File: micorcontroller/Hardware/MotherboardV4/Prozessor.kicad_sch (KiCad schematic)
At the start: 56 parts, among them J4 GSB1C41110SSHR, Y2 ABM8G-12.000MHZ-4Y-T3

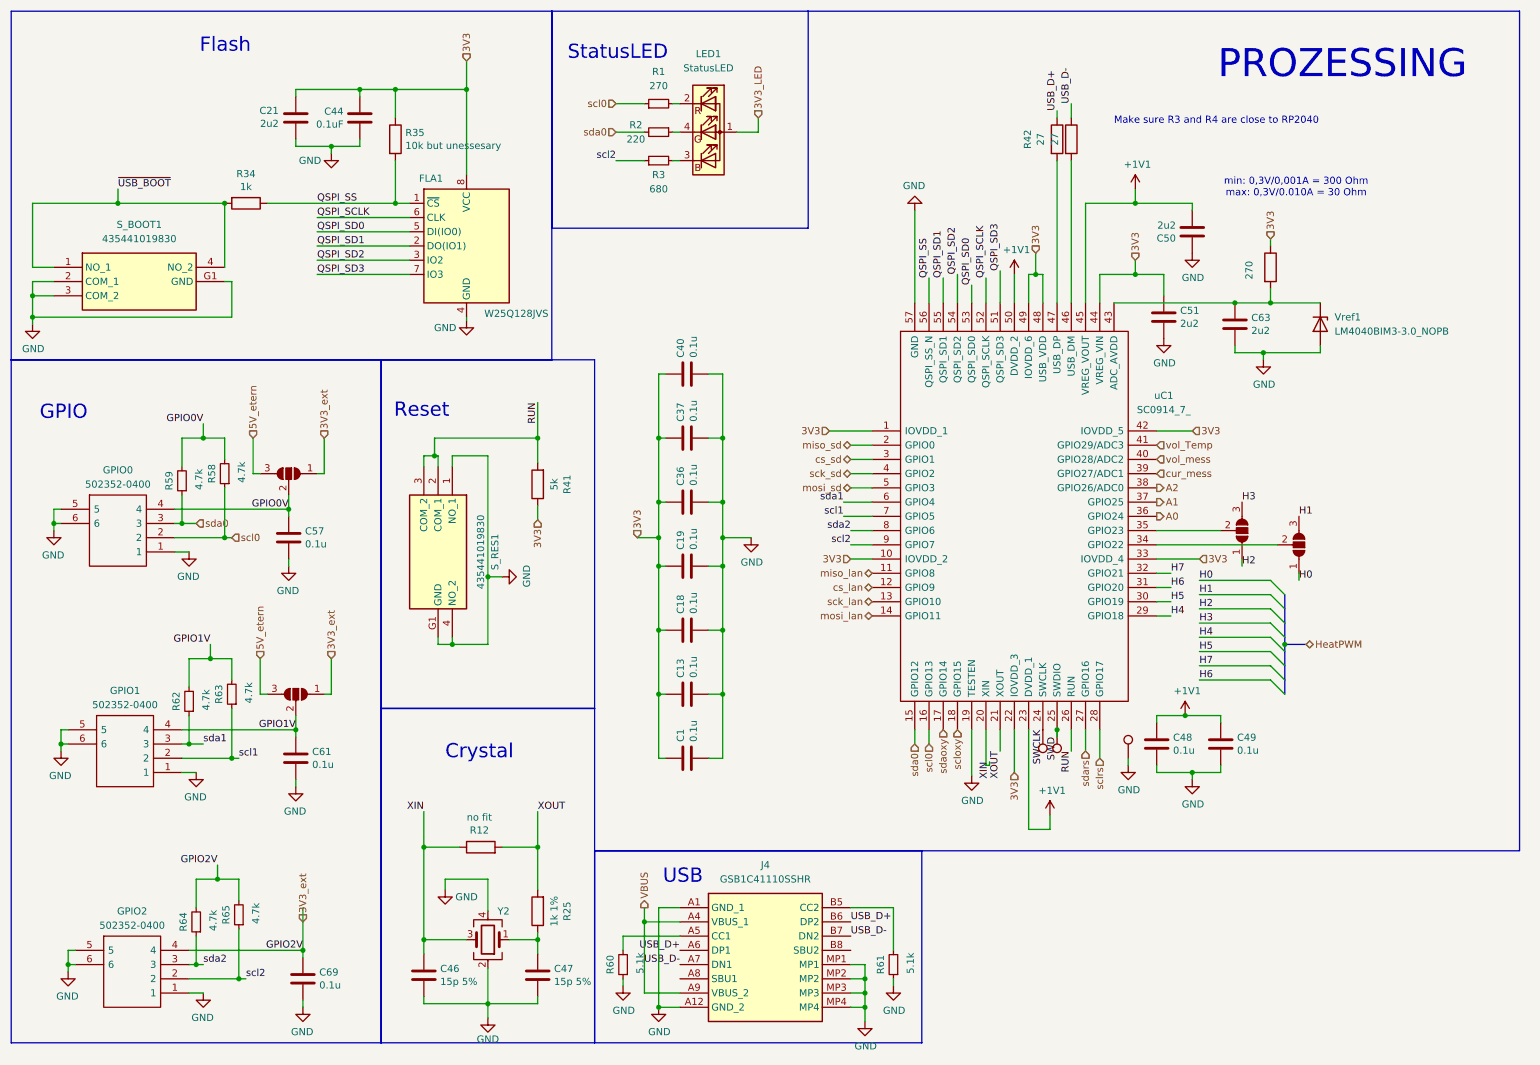
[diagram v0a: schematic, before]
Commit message: added NTC calculation
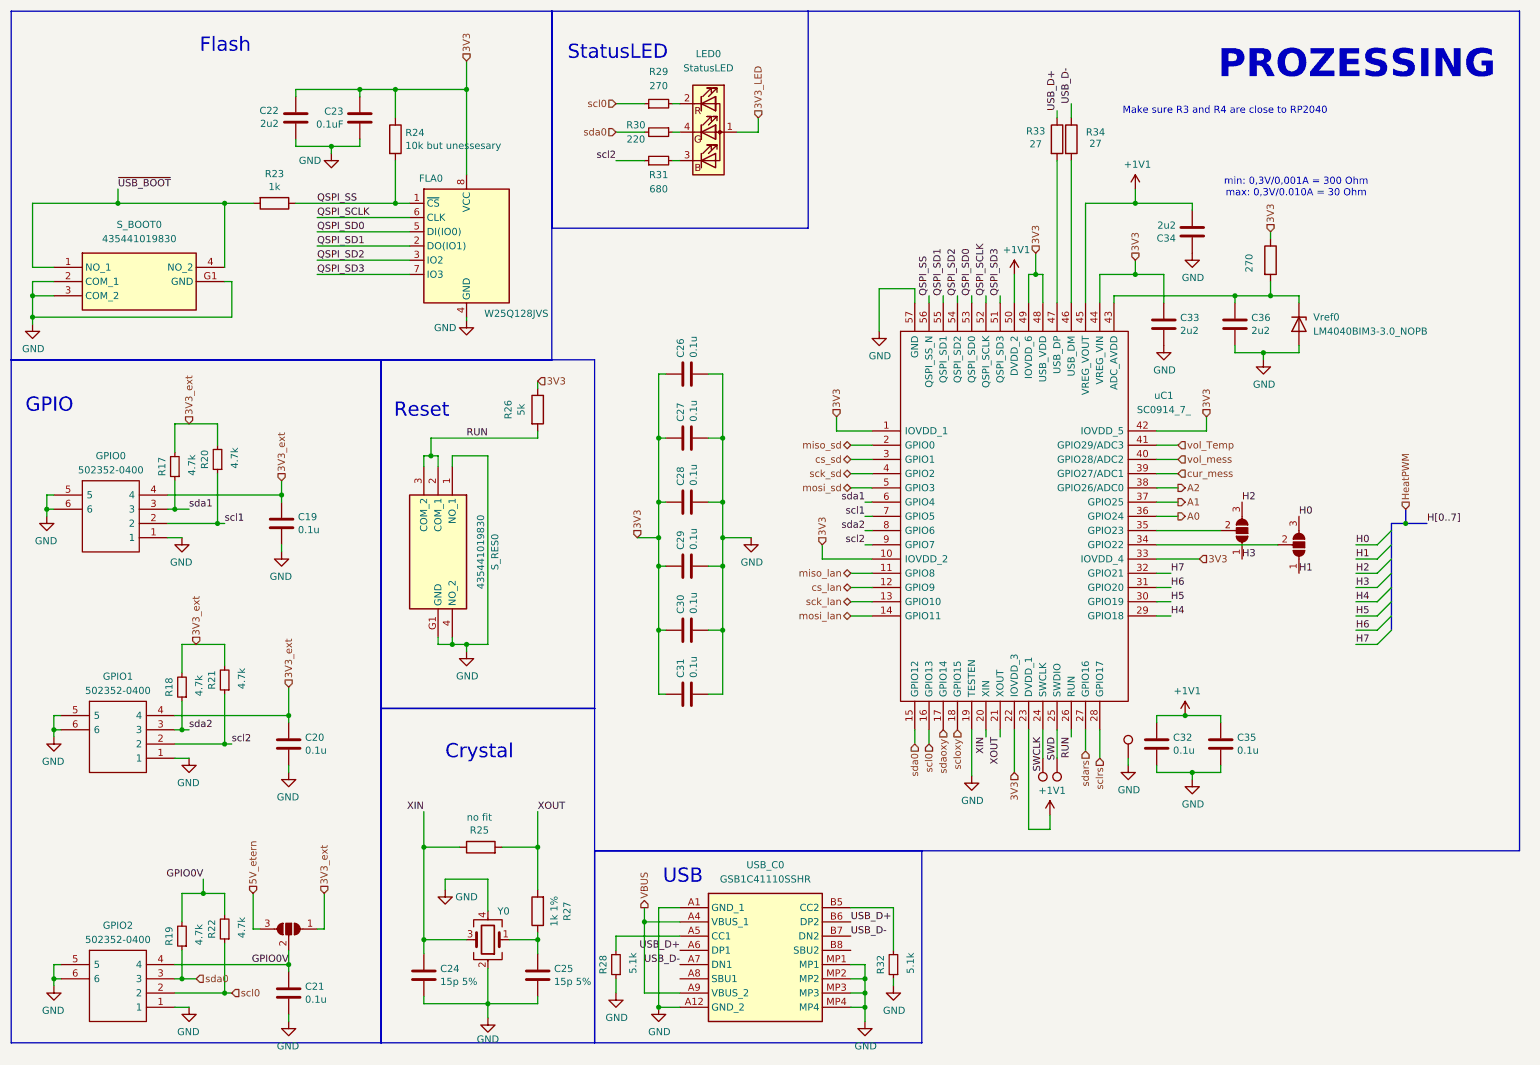
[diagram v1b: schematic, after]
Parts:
- removed C1: 0.1u, Capacitor_SMD:C_0402_1005Metric_Pad0.74x0.62mm_HandSolder, symbol Device:C
- removed JP14: SolderJumper_3_Open, Jumper:SolderJumper-3_P1.3mm_Open_RoundedPad1.0x1.5mm_NumberLabels, symbol Jumper:SolderJumper_3_Open
- renumbered C61 to C19, C69 to C20, C57 to C21, C21 to C22, C44 to C23, C46 to C24, C47 to C25, C40 to C26, C37 to C27, C36 to C28, C19 to C29, C18 to C30, C13 to C31, C48 to C32, C51 to C33, C50 to C34, C49 to C35, C63 to C36, FLA1 to FLA0, GPIO1 to GPIO0, GPIO2 to GPIO1, GPIO0 to GPIO2, JP13 to JP0, JP7 to JP1, JP15 to JP2, LED1 to LED0, R62 to R17, R64 to R18, R59 to R19, R63 to R20, R65 to R21, R58 to R22, R34 to R23, R35 to R24, R12 to R25, R41 to R26, R25 to R27, R60 to R28, R1 to R29, R2 to R30, R3 to R31, R61 to R32, R42 to R33, R43 to R34, R26 to R35, S_BOOT1 to S_BOOT0, S_RES1 to S_RES0, TP12 to TP0, TP18 to TP1, TP1 to TP2, J4 to USB_C0, Vref1 to Vref0, Y2 to Y0
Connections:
- net GPIO1V is gone; now on net 3V3_ext: C19.1, GPIO0.4, R17.2, R20.2
- net H0: now also JP2.3 (B); no longer JP2.1 (A)
- net H1: now also JP2.1 (A); no longer JP2.3 (B)
- net H2: now also JP1.3 (B); no longer JP1.1 (A)
- net H3: now also JP1.1 (A); no longer JP1.3 (B)
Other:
- moved on the sheet: C19, C20, C21, C33, GPIO0, GPIO1, GPIO2, R17, R18, R19, R20, R21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

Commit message: propper Serial Comand System added
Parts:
- R35: value 270 -> 150
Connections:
- no-connect marks 0 -> 2
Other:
- moved on the sheet: R28, R32, USB_C0

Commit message: added a serial command field for easy debugging
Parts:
- added C75: 0.1u, Capacitor_SMD:C_0402_1005Metric_Pad0.74x0.62mm_HandSolder, symbol Device:C
- added GPIO3: 502352-0400, SamacSys_Parts:5023520400, symbol SamacSys_Parts:502352-0400
- added R89, R90: 4.7k, Resistor_SMD:R_0603_1608Metric_Pad0.98x0.95mm_HandSolder, symbol Device:R_Small
- R26: value 5k -> 5.1k
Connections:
- net 3V3_ext: now also C75.1, GPIO3.4, R89.2, R90.2
- net GND: now also C75.2, GPIO3.1, GPIO3.5, GPIO3.6
- net mosi_sd: now also GPIO3.2, R90.1
- net sck_sd: now also GPIO3.3, R89.1
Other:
- moved on the sheet: C19, C20, C21, GPIO0, GPIO1, GPIO2, R17, R18, R19, R20, R21, R22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

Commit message: Switch to header BASED C file system {headache incomming}
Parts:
- renumbered C22 to C21, C19 to C22, C75 to C23, C21 to C24, C20 to C25, C23 to C26, C24 to C27, C25 to C28, C26 to C29, C27 to C30, C28 to C31, C29 to C32, C30 to C33, C31 to C34, C32 to C35, C33 to C36, C34 to C37, C35 to C38, C36 to C39, GPIO3 to GPIO1, GPIO1 to GPIO3, R17 to R16, R89 to R17, R19 to R18, R18 to R19, R90 to R21, R21 to R23, R23 to R24, R24 to R25, R25 to R26, R26 to R27, R27 to R28, R28 to R29, R29 to R30, R30 to R31, R31 to R32, R32 to R33, R33 to R34, R34 to R35, R35 to R36

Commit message: added uplink
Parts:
- C21, C22, C23, C24, C25, C26, C27, C28, C29, C30, C31, C32, C33, C34, C35, C36, C37, C38, C39: symbol Device:C -> SymbolsBalloonv4:C
- FLA0: symbol Memory_Flash:W25Q128JVS -> SymbolsBalloonv4:W25Q128JVS
- GPIO0, GPIO1, GPIO2, GPIO3: symbol SamacSys_Parts:502352-0400 -> SymbolsBalloonv4:502352-0400
- JP0, JP1, JP2: symbol Jumper:SolderJumper_3_Open -> SymbolsBalloonv4:SolderJumper_3_Open
- LED0: symbol Device:LED_ARBG -> SymbolsBalloonv4:LED_ARBG
- R16, R17, R18, R19, R20, R21, R22, R23, R29, R30, R31, R32, R33: symbol Device:R_Small -> SymbolsBalloonv4:R_Small
- R24, R25, R26, R27, R28, R34, R35, R36: symbol Device:R -> SymbolsBalloonv4:R
- S_BOOT0, S_RES0: symbol SamacSys_Parts:435441019830 -> SymbolsBalloonv4:435441019830
- TP0, TP1, TP2: symbol Connector:TestPoint -> SymbolsBalloonv4:TestPoint
- USB_C0: symbol SamacSys_Parts:GSB1C41110SSHR -> SymbolsBalloonv4:GSB1C41110SSHR
- Vref0: symbol Device:D_Zener -> SymbolsBalloonv4:D_Zener
- Y0: symbol Device:Crystal_GND24 -> SymbolsBalloonv4:Crystal_GND24
- uC1: symbol SamacSys_Parts:SC0914_7_ -> SymbolsBalloonv4:SC0914_7_
